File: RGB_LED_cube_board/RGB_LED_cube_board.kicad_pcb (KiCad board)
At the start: 2 copper layers, 100 x 100 mm, 43 parts, among them CN1 XT30UPB-M

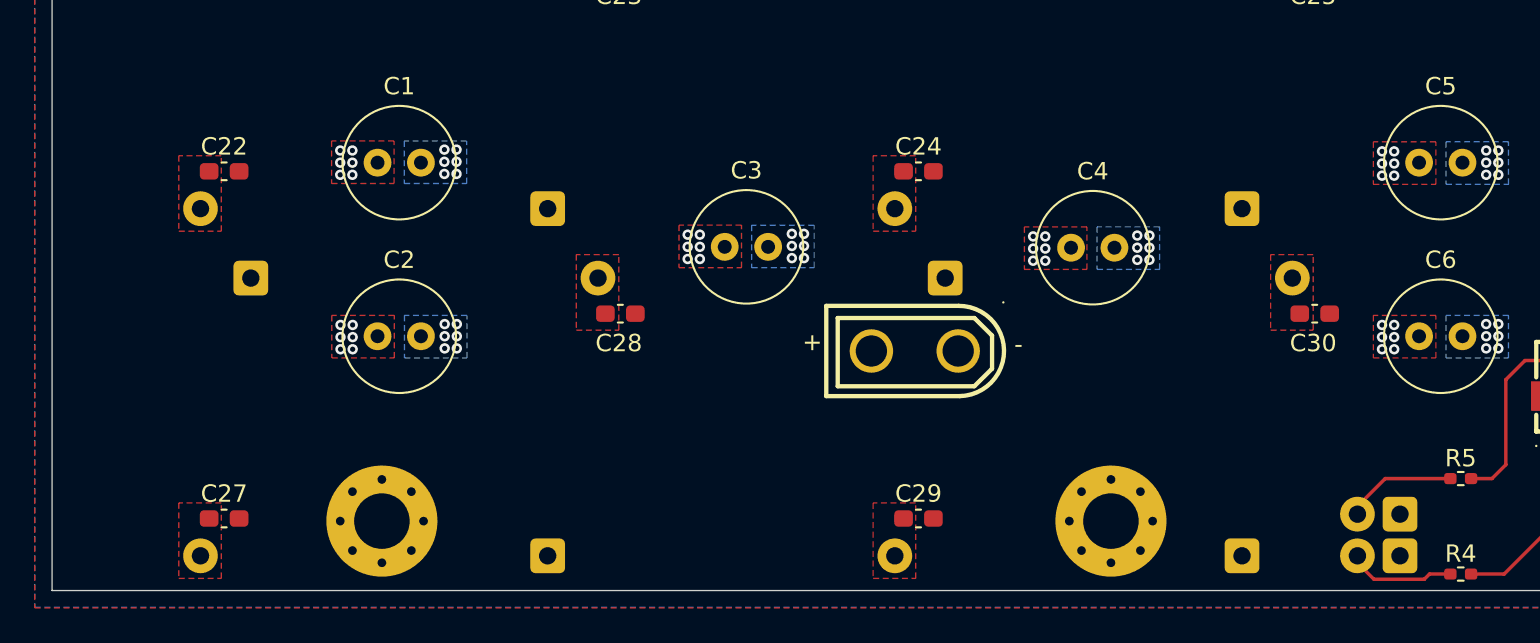
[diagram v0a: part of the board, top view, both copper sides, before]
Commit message: Small mostly cosmetic changes, followed by the export of the gerber files for production.
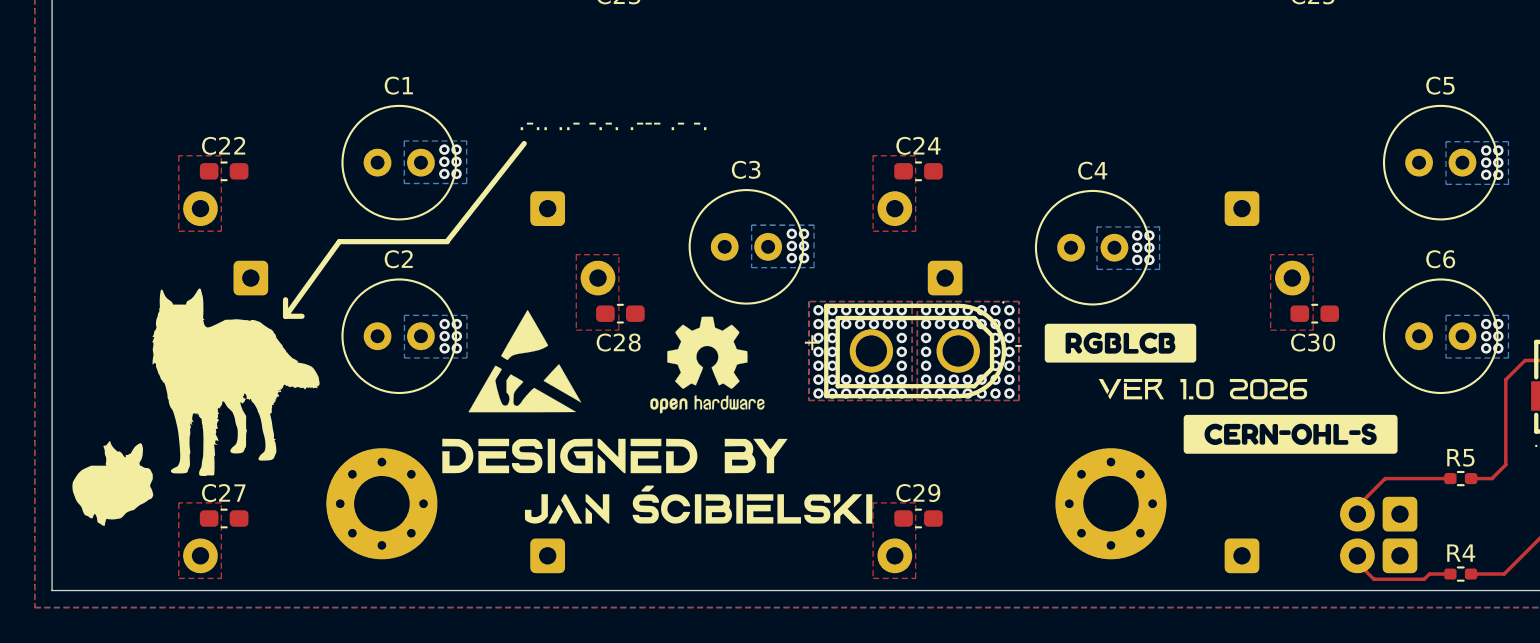
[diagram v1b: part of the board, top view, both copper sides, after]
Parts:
- added G***: LOGO, LOGO, F.Cu at (103.8, 143.6)
- added G***: LOGO, LOGO, F.Cu at (135.2, 151.3)
- added G***: LOGO, LOGO, F.Cu at (102.6, 146.5)
- added G***: LOGO, LOGO, F.Cu at (164.3, 144.4)
- added G***: LOGO, LOGO, F.Cu at (130.6, 148.2)
- added REF**: OSHW-Logo2_14.6x12mm_SilkScreen, Symbol:OSHW-Logo2_14.6x12mm_SilkScreen, F.Cu at (135.8, 143.0)
- added REF**: ESD-Logo_13.2x12mm_SilkScreen, Symbol:ESD-Logo_13.2x12mm_SilkScreen, F.Cu at (125.2, 142.8)
- added kobee-studio-6AA92370: Kobee Studio, kobee-studio-6AA92370, F.Cu at (169.3, 147.0)
- added kobee-studio-6AA9EF40: Kobee Studio, kobee-studio-6AA9EF40, F.Cu at (159.6, 141.8)
- moved H3 1.00 mm to (117.0, 151.0)
- moved H4 1.00 mm to (159.0, 151.0)
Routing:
- net VCC: vias 36 -> 37
- net GND: vias 36 -> 73
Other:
- board text added: ".-.. ..- -.-. .--- .- -."
